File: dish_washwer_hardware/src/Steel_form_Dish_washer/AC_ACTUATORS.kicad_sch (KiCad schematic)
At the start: 61 parts, among them J10 DRAIN PUMP CONNECTOR, J11 WASH PUMP CONNECTOR, J12 BOILER HEATER CONNECTOR, J13 TANK HEATER, J14 peristaltic_pump_2, J15 peristaltic_pump_1, J7 BOILER HEATER CONNECTOR, J9 SOLENOID CONNECTOR, K1 9-1440003-0, K2 9-1440003-0, K3 9-1440003-0, K4 9-1440003-0, Q3 WST2N7002K, Q4 WST2N7002K, Q5 WST2N7002K, U10 MOC3021, U11 MOC3021, U12 MOC3021, U14 9-1393243-3, U5 9-1393243-3, U6 HCPL3700M, U7 MOC3021, U8 MOC3021, U9 MOC3021

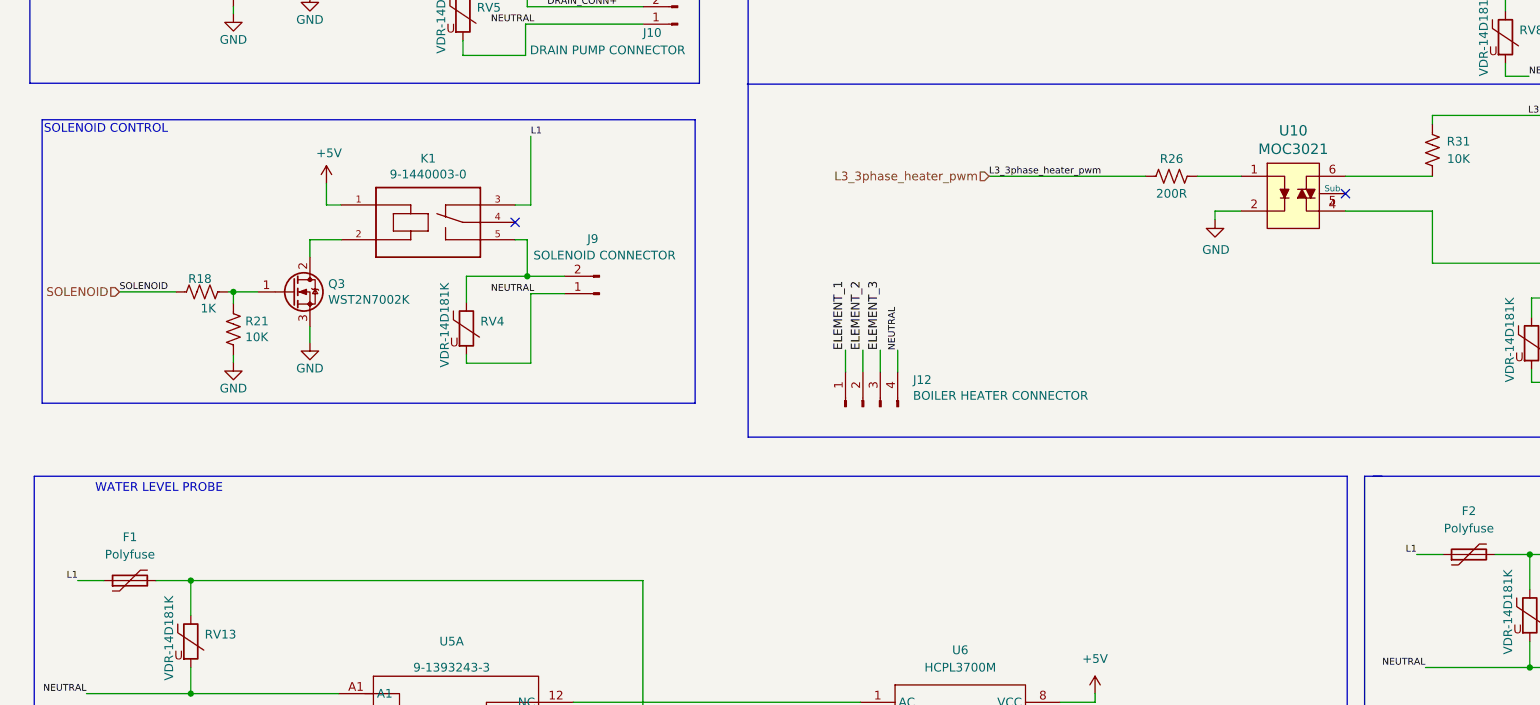
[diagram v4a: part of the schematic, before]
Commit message: layout placement complete
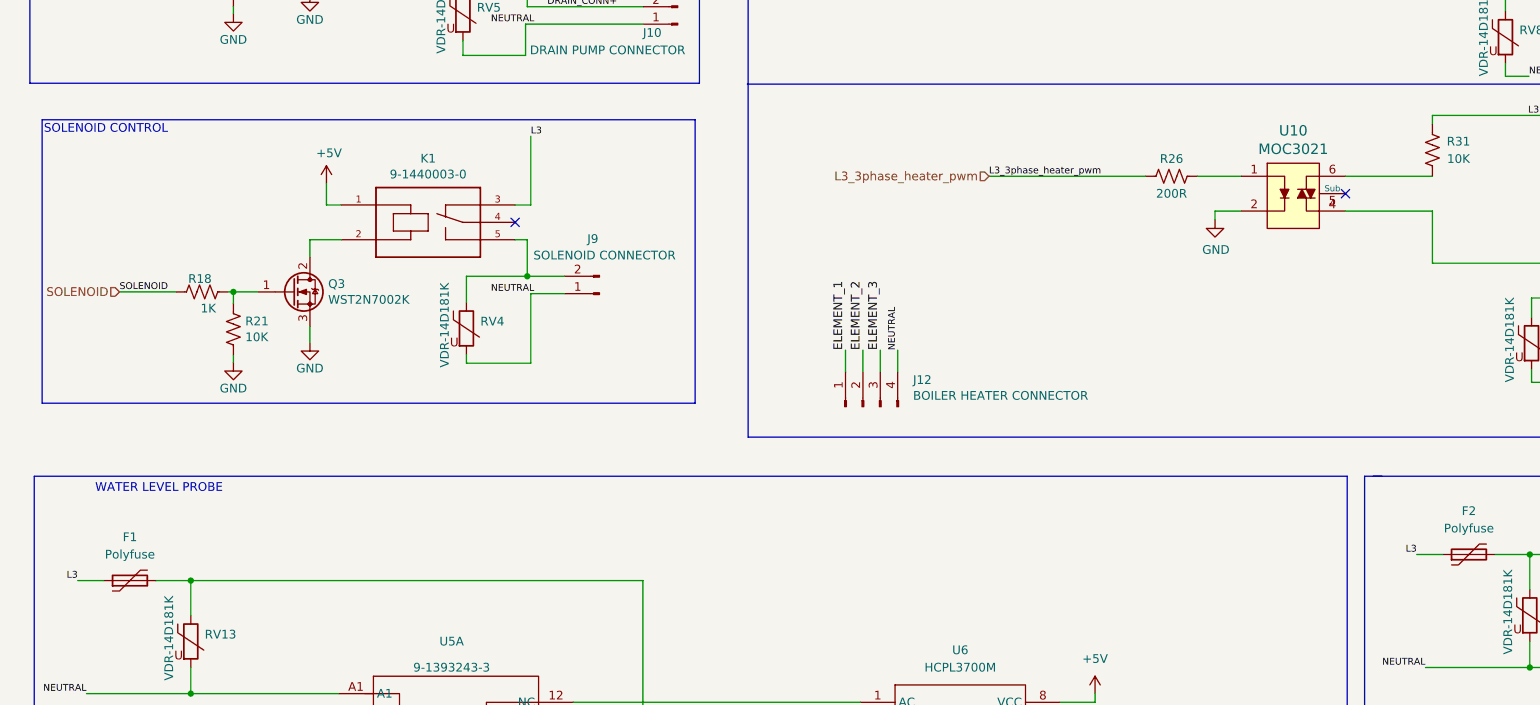
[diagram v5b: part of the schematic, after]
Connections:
- net L1: no longer F1.1, F2.1, K1.3
- net L3: now also F1.1, F2.1, K1.3
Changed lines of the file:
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@@
     (effects (font (size 0.9906 0.9906)) (justify left bottom))
   )
-  (label "L1" (at 220.98 191.77 180)
+  (label "L3" (at 220.98 191.77 180)
     (effects (font (size 0.9906 0.9906)) (justify right bottom))
   )
@@
     (effects (font (size 0.9906 0.9906)) (justify left bottom))
   )
-  (label "L1" (at 25.4 195.58 180)
+  (label "L3" (at 25.4 195.58 180)
     (effects (font (size 0.9906 0.9906)) (justify right bottom))
   )
-  (label "L1" (at 91.567 130.683 0)
+  (label "L3" (at 91.567 130.683 0)
     (effects (font (size 0.9906 0.9906)) (justify left bottom))
   )

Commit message: layout complete
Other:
- company: (none) -> STEEL FORM
- title: (none) -> DISHWASHER
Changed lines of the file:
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@@
 (kicad_sch (version 20211123) (generator eeschema)
   (paper "A3")
+  (title_block
+    (title "DISHWASHER")
+    (date "2022-02-01")
+    (rev "1")
+    (company "STEEL FORM")
+    (comment 2 "Reviewed by:")
+    (comment 3 "Designed by: Robert Mutura Macharia")
+    (comment 4 "STEEL FORM - DISHWASHER")
+  )
   (junction (at 107.95 217.17) (diameter 0) (color 0 0 0 0)
   )

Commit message: updated level connector
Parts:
- J7: value BOILER HEATER CONNECTOR -> Water sensor connector; footprint greencharge-footprints:barrier_terminal_6PCV_04_006 -> TerminalBlock_Phoenix:TerminalBlock_Phoenix_MKDS-1,5-4_1x04_P5.00mm_Horizontal
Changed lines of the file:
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@@
       (effects (font (size 1.27 1.27)) (justify right))
     )
-    (property "Value" "BOILER HEATER CONNECTOR" (id 1) (at 58.1152 243.5098 90)
+    (property "Value" "Water sensor connector" (id 1) (at 58.1152 243.5098 90)
       (effects (font (size 1.27 1.27)) (justify right))
     )
-    (property "Footprint" "greencharge-footprints:barrier_terminal_6PCV_04_006" (id 2) (at 50.8 245.11 0)
+    (property "Footprint" "TerminalBlock_Phoenix:TerminalBlock_Phoenix_MKDS-1,5-4_1x04_P5.00mm_Horizontal" (id 2) (at 50.8 245.11 0)
       (effects (font (size 1.27 1.27)) hide)
     )
